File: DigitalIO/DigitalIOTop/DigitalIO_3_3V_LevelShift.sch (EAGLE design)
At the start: 13 parts, among them K1 HF46105, K2 HF46105, K3 HF46105, K4 HF46105, Q1 691131710002, Q2 691131710002, Q3 691131710002, Q4 691131710002

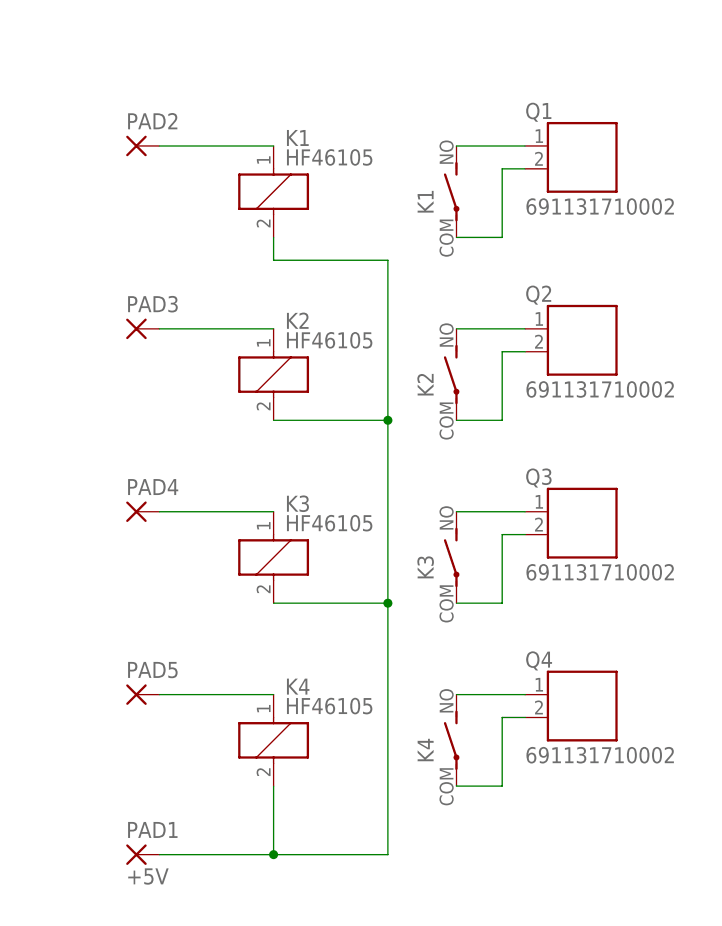
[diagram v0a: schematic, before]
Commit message: Changed some drills, pads, holes, routes and headers.
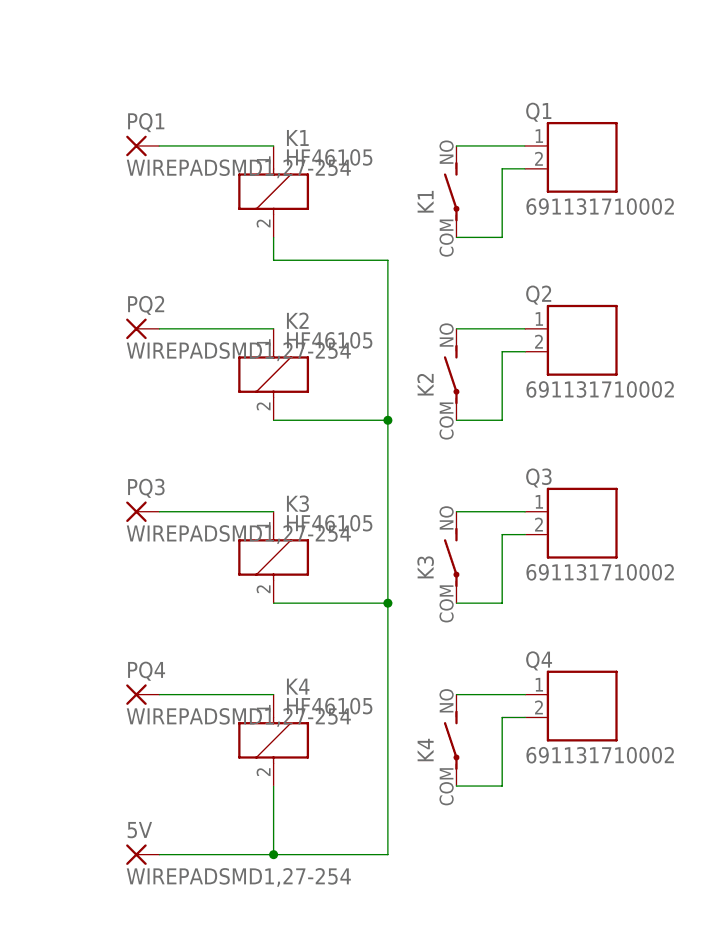
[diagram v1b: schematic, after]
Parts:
- removed PAD1: +5V, wirepad:SMD5
- removed PAD2, PAD3, PAD4, PAD5: (no value), wirepad:SMD5
- added 5V, PQ1, PQ2, PQ3, PQ4: WIREPADSMD1,27-254, wirepad:WIREPADSMD1,27-254
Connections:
- net N$1: now also 5V.P; no longer PAD1.P
- net N$14: now also PQ3.P; no longer PAD4.P
- net N$2: now also PQ2.P; no longer PAD3.P
- net N$4: now also PQ4.P; no longer PAD5.P
- net N$5: now also PQ1.P; no longer PAD2.P
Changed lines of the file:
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@@
 <part name="K3" library="hongfa" deviceset="HF46?*" device="1" technology="05"/>
 <part name="K4" library="hongfa" deviceset="HF46?*" device="1" technology="05"/>
-<part name="PAD1" library="wirepad" deviceset="SMD5" device="" value="+5V"/>
-<part name="PAD2" library="wirepad" deviceset="SMD5" device=""/>
-<part name="PAD3" library="wirepad" deviceset="SMD5" device=""/>
-<part name="PAD4" library="wirepad" deviceset="SMD5" device=""/>
-<part name="PAD5" library="wirepad" deviceset="SMD5" device=""/>
+<part name="5V" library="wirepad" deviceset="WIREPAD" device="SMD1,27-254" value="WIREPADSMD1,27-254"/>
+<part name="PQ1" library="wirepad" deviceset="WIREPAD" device="SMD1,27-254"/>
+<part name="PQ2" library="wirepad" deviceset="WIREPAD" device="SMD1,27-254"/>
+<part name="PQ3" library="wirepad" deviceset="WIREPAD" device="SMD1,27-254"/>
+<part name="PQ4" library="wirepad" deviceset="WIREPAD" device="SMD1,27-254"/>
 <part name="Q1" library="con-wuerth" deviceset="691131710002" device=""/>
 <part name="Q2" library="con-wuerth" deviceset="691131710002" device=""/>
@@
 <instance part="K4" gate="1" x="-226.06" y="73.66"/>
 <instance part="K4" gate="2" x="-205.74" y="73.66"/>
-<instance part="PAD1" gate="1" x="-241.3" y="60.96"/>
-<instance part="PAD2" gate="1" x="-241.3" y="139.7"/>
-<instance part="PAD3" gate="1" x="-241.3" y="119.38"/>
-<instance part="PAD4" gate="1" x="-241.3" y="99.06"/>
-<instance part="PAD5" gate="1" x="-241.3" y="78.74"/>
+<instance part="5V" gate="G$1" x="-241.3" y="60.96"/>
+<instance part="PQ1" gate="G$1" x="-241.3" y="139.7"/>
+<instance part="PQ2" gate="G$1" x="-241.3" y="119.38"/>
+<instance part="PQ3" gate="G$1" x="-241.3" y="99.06"/>
+<instance part="PQ4" gate="G$1" x="-241.3" y="78.74"/>
 <instance part="Q1" gate="G$1" x="-198.12" y="139.7"/>
 <instance part="Q2" gate="G$1" x="-198.12" y="119.38"/>
@@
 <junction x="-213.36" y="88.9"/>
 <wire x1="-226.06" y1="60.96" x2="-238.76" y2="60.96" width="0.1524" layer="91"/>
-<pinref part="PAD1" gate="1" pin="P"/>
+<pinref part="5V" gate="G$1" pin="P"/>
 <junction x="-226.06" y="60.96"/>
 <pinref part="K2" gate="1" pin="2"/>
@@
 <pinref part="K2" gate="1" pin="1"/>
 <wire x1="-226.06" y1="119.38" x2="-238.76" y2="119.38" width="0.1524" layer="91"/>
-<pinref part="PAD3" gate="1" pin="P"/>
+<pinref part="PQ2" gate="G$1" pin="P"/>
 </segment>
 </net>
@@
 <pinref part="K4" gate="1" pin="1"/>
 <wire x1="-226.06" y1="78.74" x2="-238.76" y2="78.74" width="0.1524" layer="91"/>
-<pinref part="PAD5" gate="1" pin="P"/>
+<pinref part="PQ4" gate="G$1" pin="P"/>
 </segment>
 </net>
@@
 <pinref part="K1" gate="1" pin="1"/>
 <wire x1="-226.06" y1="139.7" x2="-238.76" y2="139.7" width="0.1524" layer="91"/>
-<pinref part="PAD2" gate="1" pin="P"/>
+<pinref part="PQ1" gate="G$1" pin="P"/>
 </segment>
 </net>
@@
 <net name="N$14" class="0">
 <segment>
-<pinref part="PAD4" gate="1" pin="P"/>
+<pinref part="PQ3" gate="G$1" pin="P"/>
 <pinref part="K3" gate="1" pin="1"/>
 <wire x1="-238.76" y1="99.06" x2="-226.06" y2="99.06" width="0.1524" layer="91"/>

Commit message: Add ground plane on top pcb.
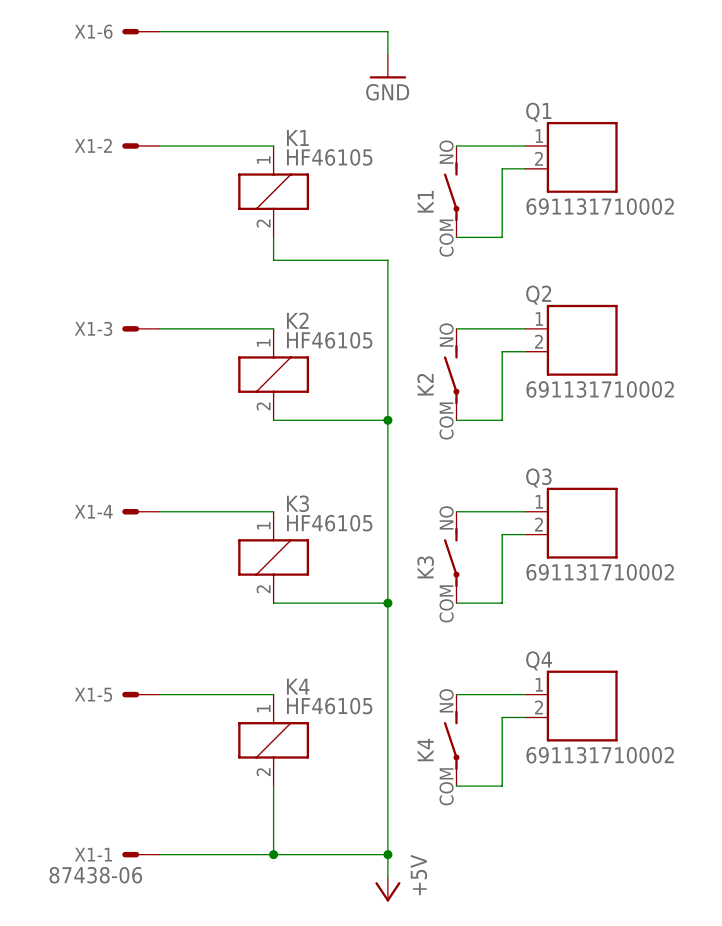
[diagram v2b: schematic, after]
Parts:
- removed 5V, PQ1, PQ2, PQ3, PQ4: WIREPADSMD1,27-254, wirepad:WIREPADSMD1,27-254
- added X1: 87438-06, con-molex:87438-06
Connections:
- removed net N$1: 5V.P, K11.2, K21.2, K31.2, K41.2
- new net +5V: K11.2, K21.2, K31.2, K41.2, X1-1.S
- new net GND: X1-6.S
- net N$14: now also X1-4.S; no longer PQ3.P
- net N$2: now also X1-3.S; no longer PQ2.P
- net N$4: now also X1-5.S; no longer PQ4.P
- net N$5: now also X1-2.S; no longer PQ1.P
